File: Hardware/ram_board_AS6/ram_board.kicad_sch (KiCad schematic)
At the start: 12 parts, among them J1 Conn_01x40, U1 74HC00, U2 74HC04, U4 74HC02, U5 74HC273, U6 AS6C4008-55PCN

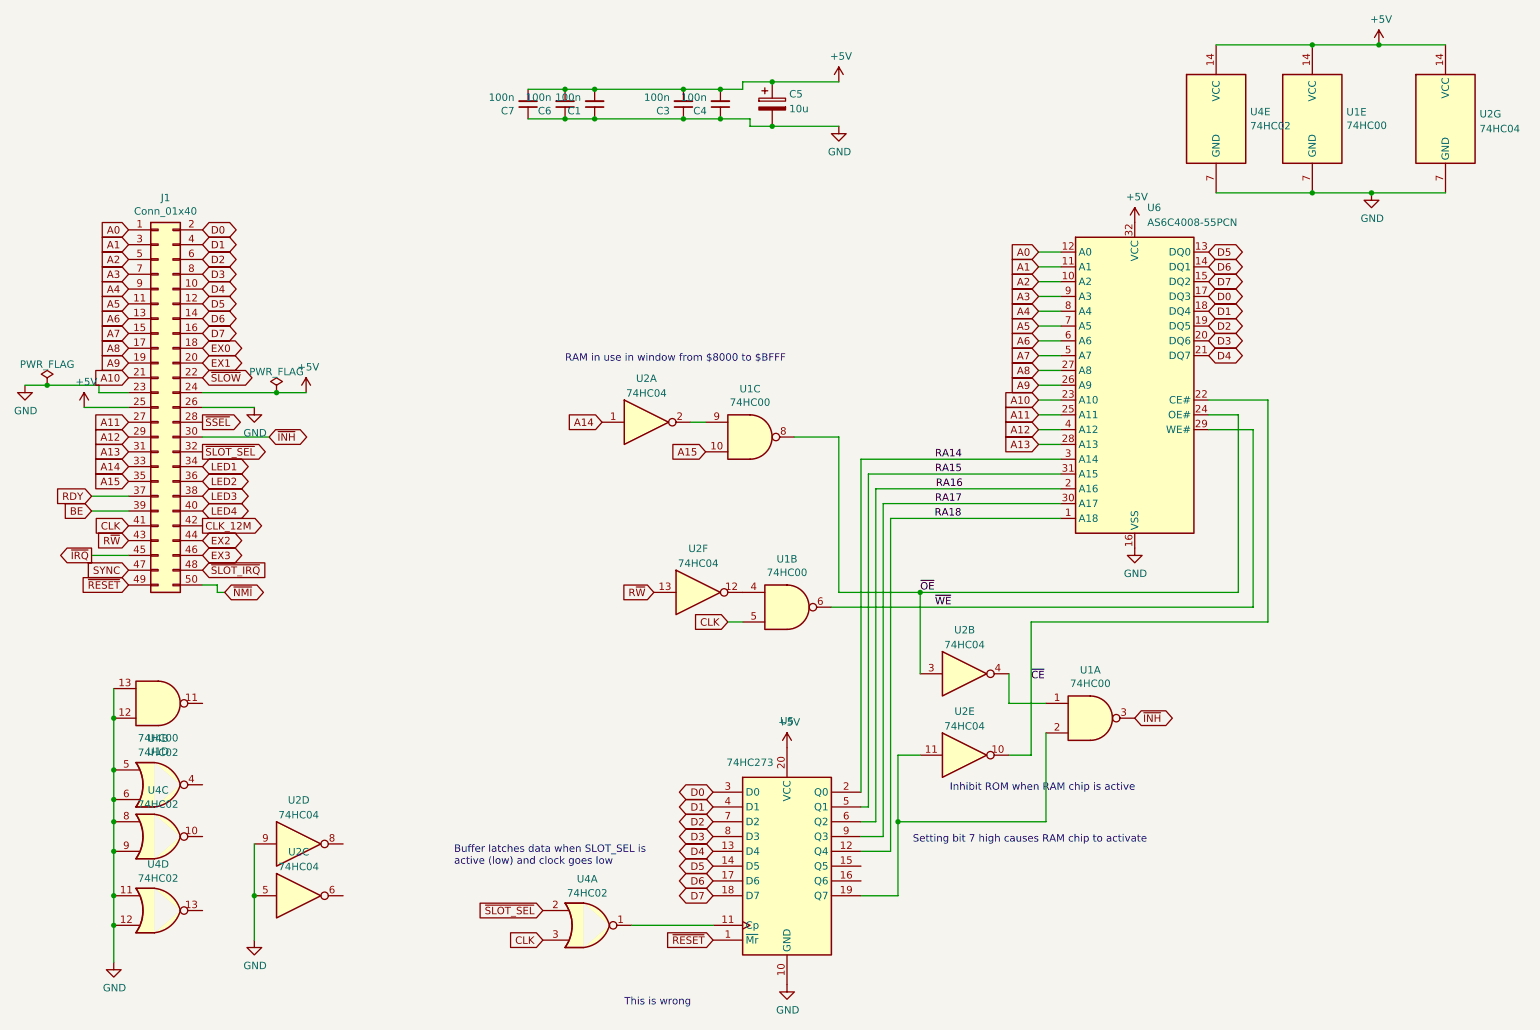
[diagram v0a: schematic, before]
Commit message: WRITE signal now ative when writing to memmory window
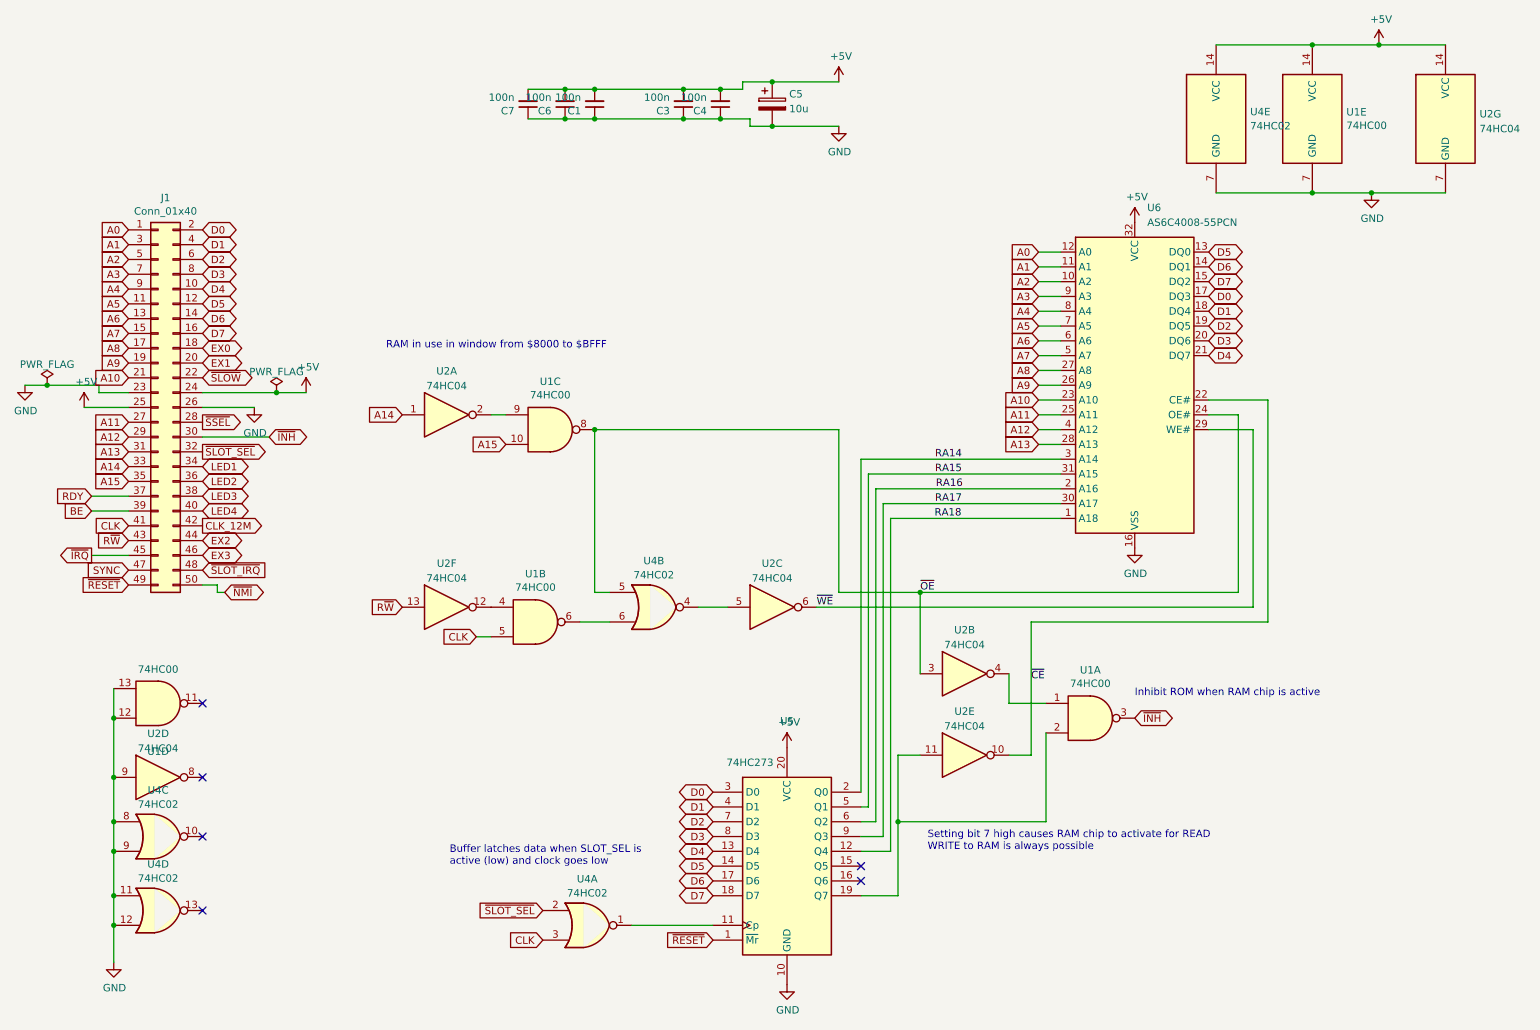
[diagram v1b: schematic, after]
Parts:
- C1, C3, C4, C5, C6, C7: KiLib_Generator (none) -> capacitor/THT/other
- J1: KiLib_Generator (none) -> connector/pin_header_socket
- U1, U2, U4, U5, U6: KiLib_Generator (none) -> package/DIP/legacy
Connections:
- net GND: no longer U2.5, U4.5, U4.6
- net ~{OE}: now also U4.5
- net ~{WE}: now also U2.6; no longer U1.6
- net at U4.4: now also U2.5
- new net: U1.6, U4.6
- no-connect marks 0 -> 6
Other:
- note added: "Setting bit 7 high causes RAM chip to activate for READ WRITE to RAM is always possible"
- note removed: "Setting bit 7 high causes RAM chip to activate"
- note removed: "This is wrong"
- company: Six Pixels -> Lexx
- title: RAM Board -> AS6 RAM Board
- moved on the sheet: U1B, U1C, U2A, U2C, U2D, U2F, U4B
